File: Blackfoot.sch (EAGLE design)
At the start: 60 parts, among them IC1 ATMEGA644M, J1 CONN_4SCREW_2.54, J2 CONN_6, Q1 MOSFET_PCH-IRLML2244, Q2 MOSFET-NCH-DMG3404L, Q5 MOSFET_PCH-IRLML2244, U2 FT231X-Q

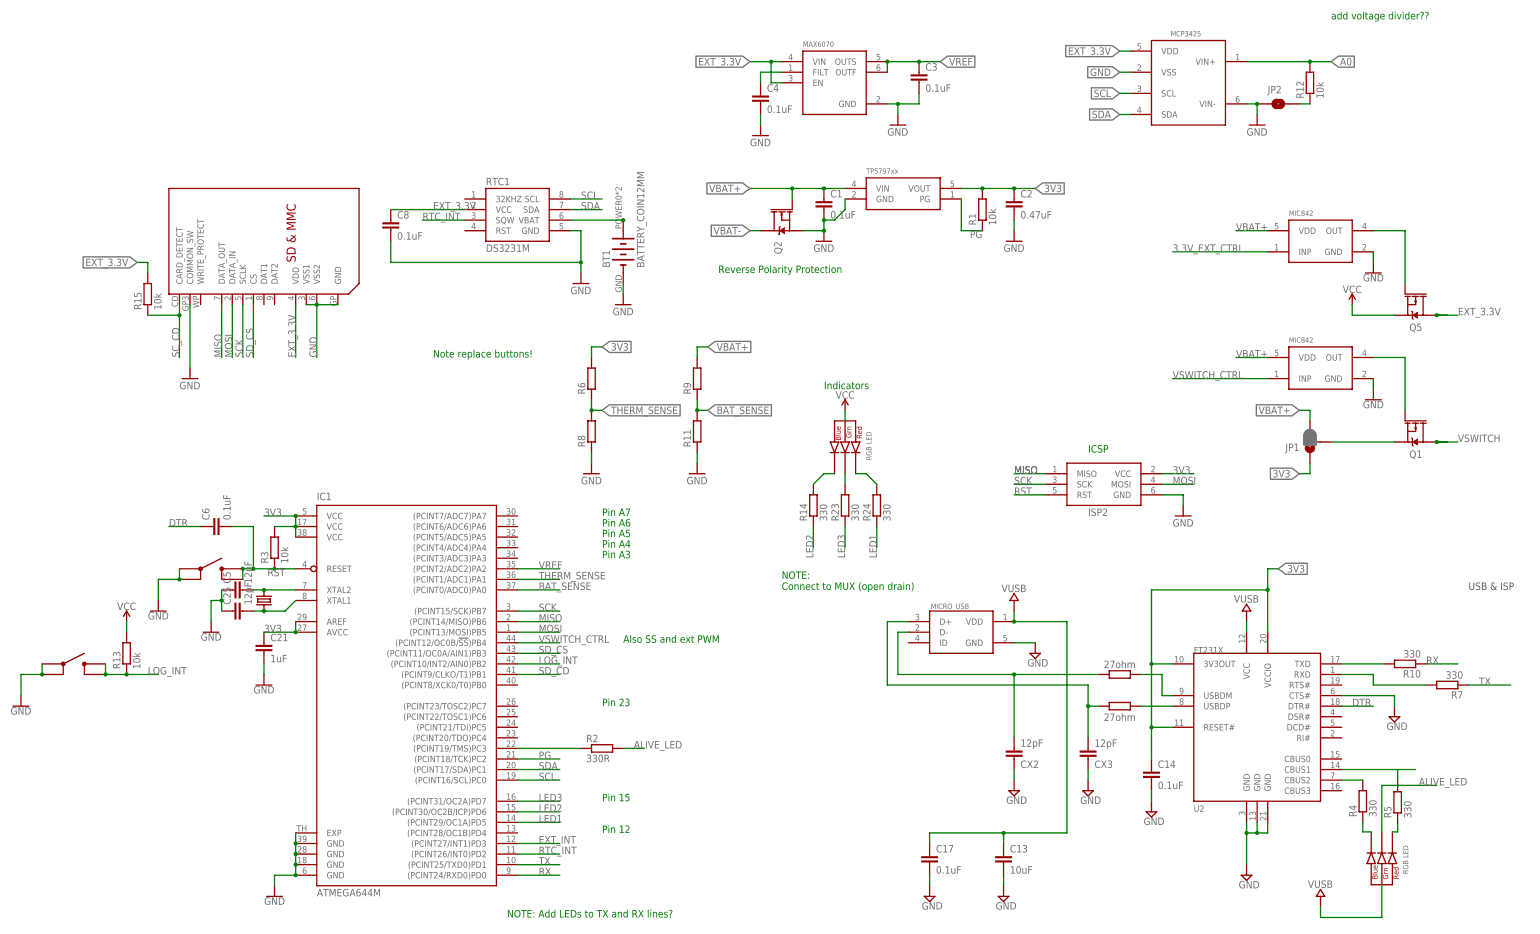
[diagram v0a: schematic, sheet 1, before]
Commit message: Preliminary layout done, fixed led issue
Finished with first round layout, changed supply voltage for LEDs to be 3v3 instead of VUSB so that alive led can work regardless of use of USB voltage
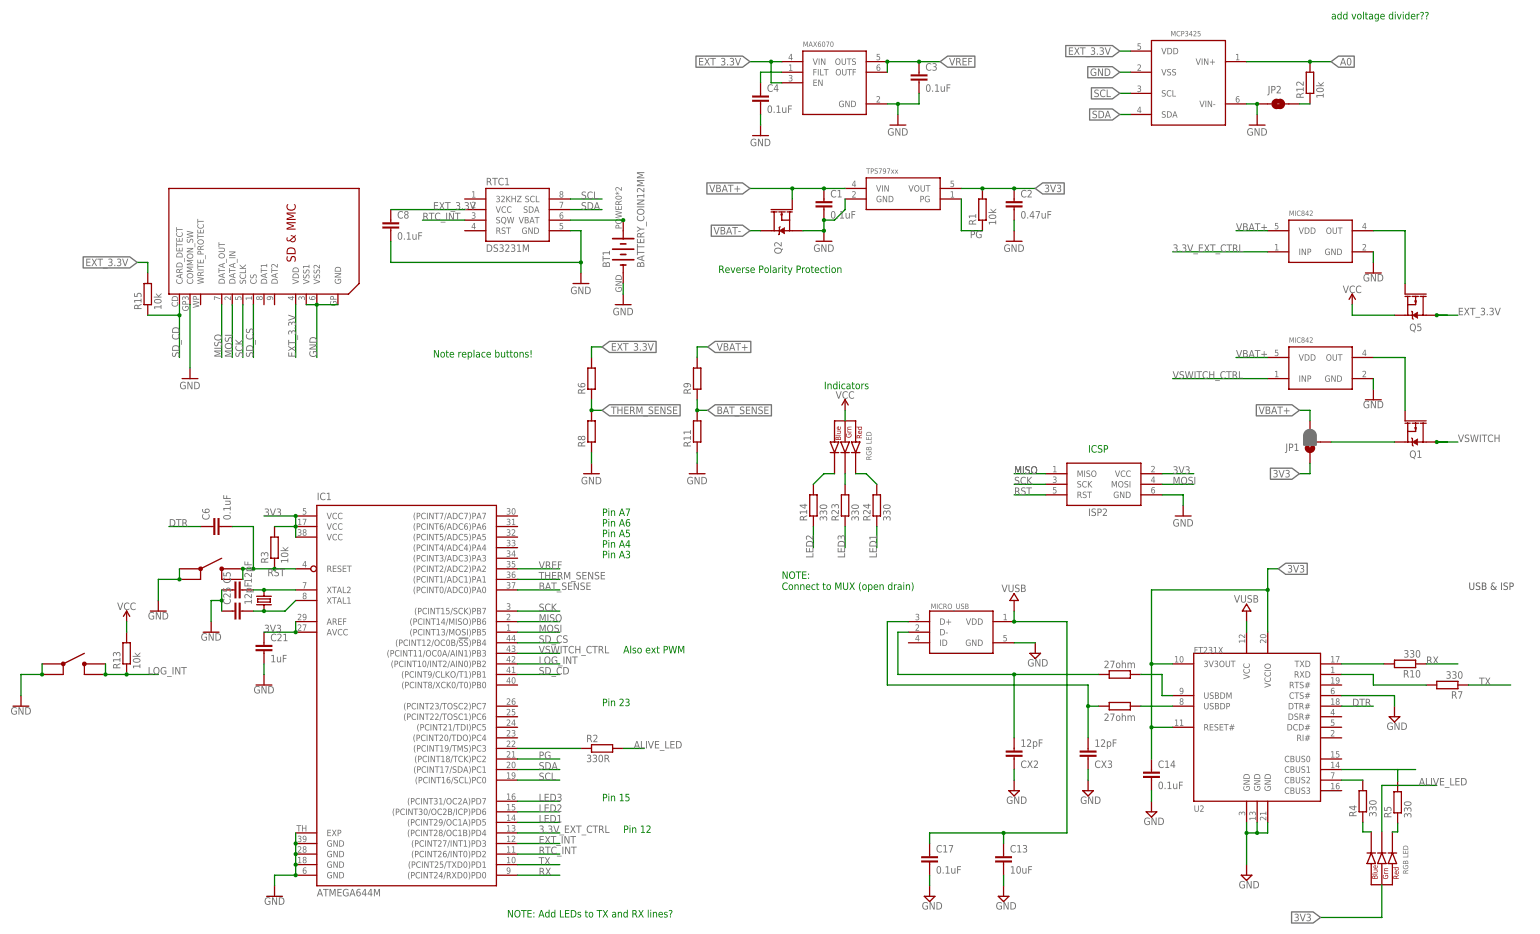
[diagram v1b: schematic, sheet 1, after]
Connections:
- removed net SC_CD: R15.1, U$3.CARD_DETECT
- net 3.3V_EXT_CTRL: now also IC1.(PCINT28/OC1B)PD4
- net 3V3: now also U$16.ANODE; no longer R6.2
- net EXT_3.3V: now also R6.2
- net SD_CD: now also R15.1, U$3.CARD_DETECT
- net SD_CS: now also IC1.(PCINT12/OC0B/!SS!)PB4; no longer IC1.(PCINT11/OC0A/AIN1)PB3
- net VSWITCH_CTRL: now also IC1.(PCINT11/OC0A/AIN1)PB3; no longer IC1.(PCINT12/OC0B/!SS!)PB4
- net VUSB: no longer U$16.ANODE
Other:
- note added: "Also ext PWM"
- note removed: "Also SS and ext PWM"
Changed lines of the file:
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@@
 <part name="SUPPLY33" library="supply2" library_urn="urn:adsk.eagle:library:372" deviceset="GND" device=""/>
 <part name="SUPPLY36" library="supply2" library_urn="urn:adsk.eagle:library:372" deviceset="GND" device=""/>
-<part name="U$12" library="MyPOW" deviceset="VUSB" device=""/>
 <part name="SUPPLY48" library="supply2" library_urn="urn:adsk.eagle:library:372" deviceset="GND" device=""/>
 <part name="SUPPLY49" library="supply2" library_urn="urn:adsk.eagle:library:372" deviceset="GND" device=""/>
@@
 <part name="C8" library="bschulz" deviceset="C-EU" device="C0603" value="0.1uF"/>
 <part name="U$20" library="MyPOW" deviceset="VUSB" device=""/>
-<part name="U$3" library="adafruit" deviceset="SDMMC" device="06132"/>
+<part name="U$3" library="adafruit" library_urn="urn:adsk.eagle:library:420" deviceset="SDMMC" device="06132"/>
 <part name="Q5" library="bschulz" deviceset="MOSFET_PCH" device="-IRLML2244" value="MOSFET_PCH-IRLML2244"/>
 <part name="SUPPLY10" library="SparkFun-PowerSymbols" deviceset="VCC" device=""/>
@@
 Connect to MUX (open drain)</text>
 <text x="111.76" y="149.86" size="1.778" layer="91">Note replace buttons!</text>
-<text x="152.4" y="35.56" size="1.778" layer="91">Pin 12</text>
+<text x="157.48" y="35.56" size="1.778" layer="91">Pin 12</text>
 <text x="152.4" y="111.76" size="1.778" layer="91">Pin A7</text>
 <text x="152.4" y="109.22" size="1.778" layer="91">Pin A6</text>
@@
 <text x="152.4" y="66.04" size="1.778" layer="91">Pin 23</text>
 <text x="152.4" y="101.6" size="1.778" layer="91">Pin A3</text>
-<text x="157.48" y="81.28" size="1.778" layer="91">Also SS and ext PWM</text>
+<text x="157.48" y="78.74" size="1.778" layer="91">Also ext PWM</text>
 <text x="269.24" y="127" size="1.778" layer="91">ICSP</text>
 <text x="327.66" y="231.14" size="1.778" layer="91">add voltage divider??</text>
@@
 <instance part="SUPPLY33" gate="GND" x="342.9" y="63.5"/>
 <instance part="SUPPLY36" gate="GND" x="256.54" y="78.74"/>
-<instance part="U$12" gate="G$1" x="325.12" y="20.32"/>
 <instance part="SUPPLY48" gate="GND" x="248.92" y="20.32"/>
 <instance part="SUPPLY49" gate="GND" x="231.14" y="20.32"/>
@@
 </segment>
 <segment>
-<pinref part="R6" gate="G$1" pin="2"/>
-<wire x1="149.86" y1="149.86" x2="149.86" y2="152.4" width="0.1524" layer="91"/>
-<wire x1="149.86" y1="152.4" x2="152.4" y2="152.4" width="0.1524" layer="91"/>
-<label x="152.4" y="152.4" size="1.778" layer="95" xref="yes"/>
-</segment>
-<segment>
 <pinref part="ISP2" gate="G$1" pin="VCC"/>
 <wire x1="287.02" y1="121.92" x2="294.64" y2="121.92" width="0.1524" layer="91"/>
 <label x="289.56" y="121.92" size="1.778" layer="95"/>
+</segment>
+<segment>
+<wire x1="339.852" y1="15.24" x2="325.12" y2="15.24" width="0.1524" layer="91"/>
+<pinref part="U$16" gate="G$1" pin="ANODE"/>
+<wire x1="339.852" y1="23.114" x2="339.852" y2="15.24" width="0.1524" layer="91"/>
+<label x="325.12" y="15.24" size="1.778" layer="95" rot="R180" xref="yes"/>
 </segment>
 </net>
@@
 </segment>
 <segment>
-<pinref part="IC1" gate="G$1" pin="(PCINT11/OC0A/AIN1)PB3"/>
-<wire x1="132.08" y1="78.74" x2="142.24" y2="78.74" width="0.1524" layer="91"/>
-<label x="137.16" y="78.74" size="1.778" layer="95"/>
+<pinref part="IC1" gate="G$1" pin="(PCINT12/OC0B/!SS!)PB4"/>
+<wire x1="132.08" y1="81.28" x2="142.24" y2="81.28" width="0.1524" layer="91"/>
+<label x="137.16" y="81.28" size="1.778" layer="95"/>
 </segment>
 </net>
@@
 <wire x1="132.08" y1="73.66" x2="142.24" y2="73.66" width="0.1524" layer="91"/>
 <label x="137.16" y="73.66" size="1.778" layer="95"/>
+</segment>
+<segment>
+<pinref part="U$3" gate="G$1" pin="CARD_DETECT"/>
+<wire x1="50.8" y1="162.56" x2="50.8" y2="160.02" width="0.1524" layer="91"/>
+<label x="50.8" y="149.86" size="1.778" layer="95" rot="R90"/>
+<pinref part="R15" gate="G$1" pin="1"/>
+<wire x1="50.8" y1="160.02" x2="50.8" y2="149.86" width="0.1524" layer="91"/>
+<wire x1="43.18" y1="160.02" x2="50.8" y2="160.02" width="0.1524" layer="91"/>
+<junction x="50.8" y="160.02"/>
 </segment>
 </net>
@@
 <wire x1="307.34" y1="86.36" x2="307.34" y2="83.82" width="0.1524" layer="91"/>
 </segment>
-<segment>
-<wire x1="339.852" y1="15.24" x2="325.12" y2="15.24" width="0.1524" layer="91"/>
-<wire x1="325.12" y1="15.24" x2="325.12" y2="17.78" width="0.1524" layer="91"/>
-<pinref part="U$12" gate="G$1" pin="VUSB"/>
-<pinref part="U$16" gate="G$1" pin="ANODE"/>
-<wire x1="339.852" y1="23.114" x2="339.852" y2="15.24" width="0.1524" layer="91"/>
-</segment>
 </net>
 <net name="N$40" class="0">
@@
 <label x="40.64" y="172.72" size="1.778" layer="95" rot="R180" xref="yes"/>
 </segment>
-</net>
-<net name="SC_CD" class="0">
-<segment>
-<pinref part="U$3" gate="G$1" pin="CARD_DETECT"/>
-<wire x1="50.8" y1="162.56" x2="50.8" y2="160.02" width="0.1524" layer="91"/>
-<label x="50.8" y="149.86" size="1.778" layer="95" rot="R90"/>
-<pinref part="R15" gate="G$1" pin="1"/>
-<wire x1="50.8" y1="160.02" x2="50.8" y2="149.86" width="0.1524" layer="91"/>
-<wire x1="43.18" y1="160.02" x2="50.8" y2="160.02" width="0.1524" layer="91"/>
-<junction x="50.8" y="160.02"/>
+<segment>
+<pinref part="R6" gate="G$1" pin="2"/>
+<wire x1="149.86" y1="149.86" x2="149.86" y2="152.4" width="0.1524" layer="91"/>
+<wire x1="149.86" y1="152.4" x2="152.4" y2="152.4" width="0.1524" layer="91"/>
+<label x="152.4" y="152.4" size="1.778" layer="95" xref="yes"/>
 </segment>
 </net>
@@
 <wire x1="312.42" y1="175.26" x2="289.56" y2="175.26" width="0.1524" layer="91"/>
 <label x="289.56" y="175.26" size="1.778" layer="95"/>
+</segment>
+<segment>
+<pinref part="IC1" gate="G$1" pin="(PCINT28/OC1B)PD4"/>
+<wire x1="132.08" y1="35.56" x2="142.24" y2="35.56" width="0.1524" layer="91"/>
+<label x="137.16" y="35.56" size="1.778" layer="95"/>
 </segment>
 </net>
@@
 </segment>
 <segment>
-<pinref part="IC1" gate="G$1" pin="(PCINT12/OC0B/!SS!)PB4"/>
-<wire x1="132.08" y1="81.28" x2="142.24" y2="81.28" width="0.1524" layer="91"/>
-<label x="137.16" y="81.28" size="1.778" layer="95"/>
-</segment>
-</net>
+<pinref part="IC1" gate="G$1" pin="(PCINT11/OC0A/AIN1)PB3"/>
+<wire x1="132.08" y1="78.74" x2="142.24" y2="78.74" width="0.1524" layer="91"/>
+<label x="137.16" y="78.74" size="1.778" layer="95"/>
+</segment>
+</net>
